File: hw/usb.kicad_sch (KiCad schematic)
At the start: 25 parts, among them J4 USB_C_Receptacle, U7 CAT24C128, U8 USBLC6-2SC6, U9 CY7C68013A-56PVX, Y1 24MHz

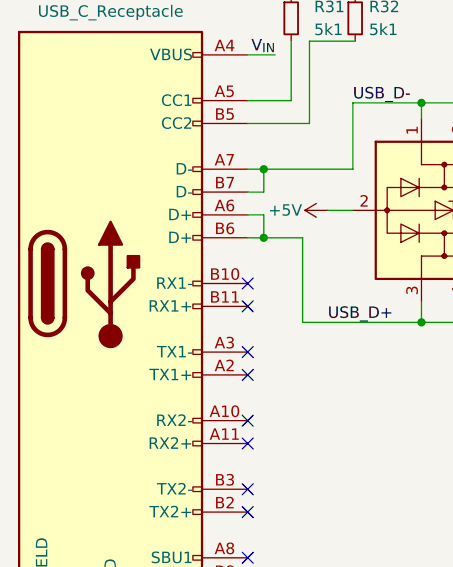
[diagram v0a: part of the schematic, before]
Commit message: schematic fixes and adding sw section
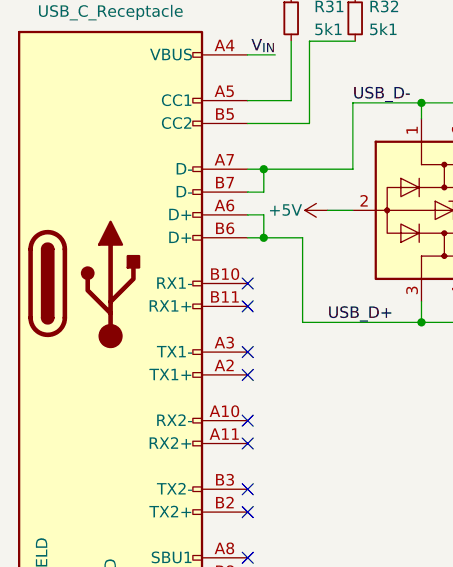
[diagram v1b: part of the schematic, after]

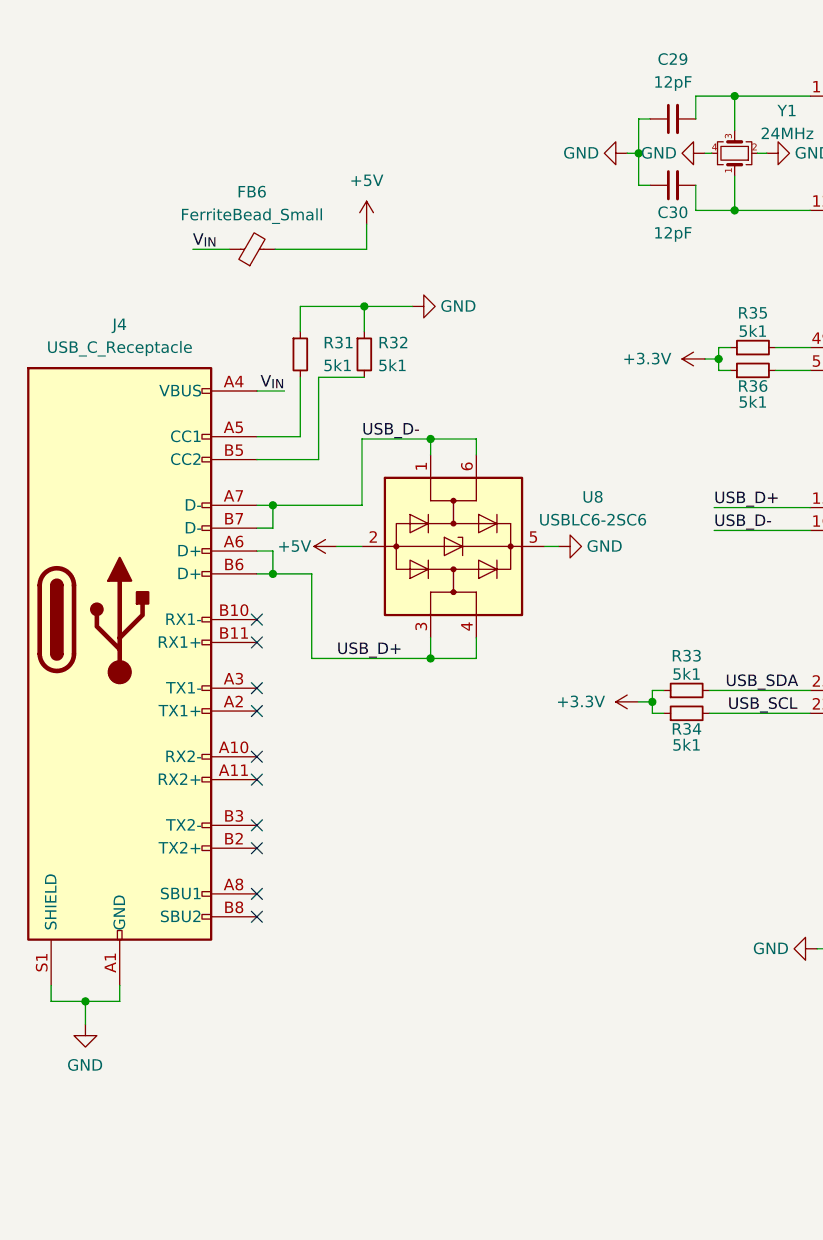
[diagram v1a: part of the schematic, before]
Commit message: working UVC demo
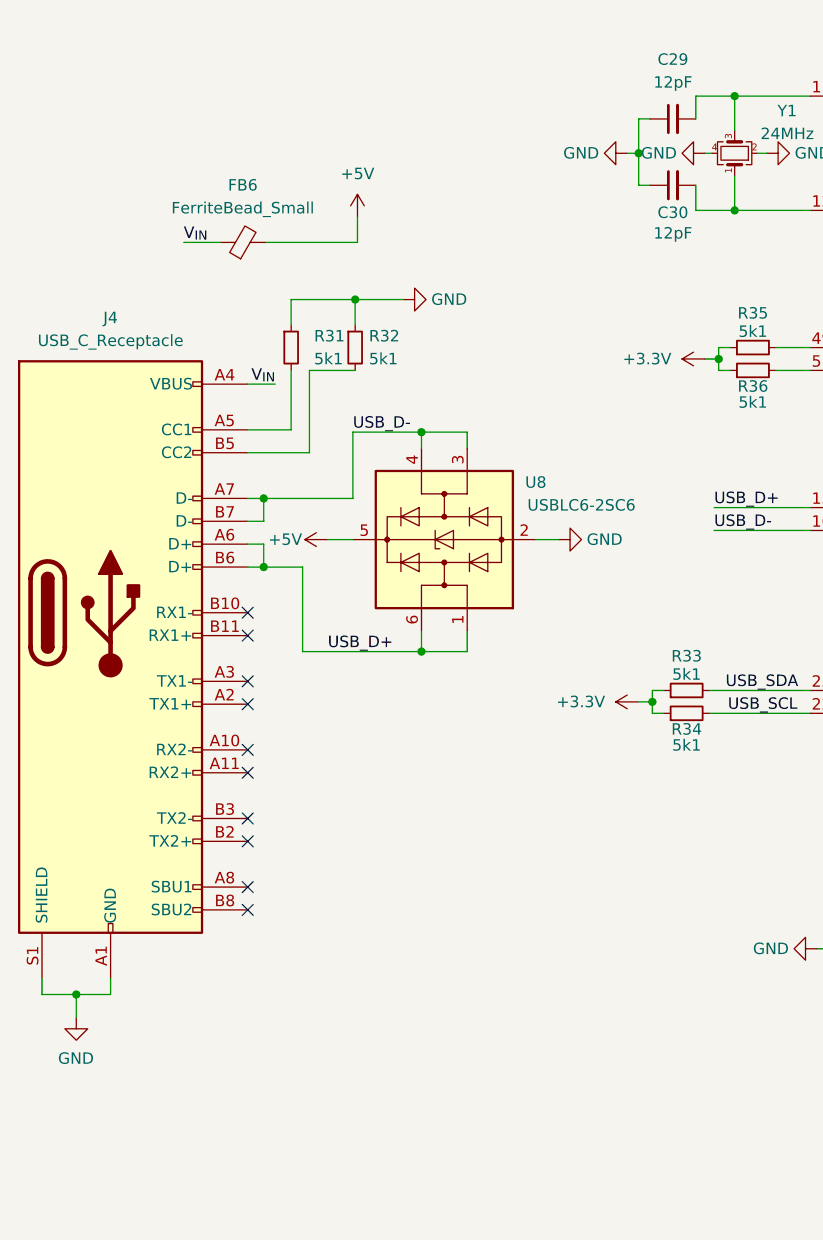
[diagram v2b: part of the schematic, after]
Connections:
- net +5V: now also U8.5 (VBUS); no longer U8.2 (GND)
- net GND: now also U8.2 (GND); no longer U8.5 (VBUS)
- net USB_D+: now also U8.1 (I/O1), U8.6 (I/O1); no longer U8.3 (I/O2), U8.4 (I/O2)
- net USB_D-: now also U8.3 (I/O2), U8.4 (I/O2); no longer U8.1 (I/O1), U8.6 (I/O1)
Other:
- moved on the sheet: FB6, J4, R31, R32, U8
